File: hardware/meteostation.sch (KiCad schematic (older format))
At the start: 19 parts

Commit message: Annotation complete
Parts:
- gave numbers to parts that had none: 19
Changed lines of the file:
@@
 $EndDescr
 $Comp
-L Device:C C?
+L Device:C C7
 U 1 1 6032A8FA
 P 10250 3050
-F 0 "C?" H 10365 3096 50  0000 L CNN
+F 0 "C7" H 10365 3096 50  0000 L CNN
 F 1 "100nF" H 10365 3005 50  0000 L CNN
 F 2 "" H 10288 2900 50  0001 C CNN
@@
 $EndComp
 $Comp
-L power:GND #PWR0103
+L power:GND #PWR017
 U 1 1 6032C2F4
 P 10250 3300
-F 0 "#PWR0103" H 10250 3050 50  0001 C CNN
+F 0 "#PWR017" H 10250 3050 50  0001 C CNN
 F 1 "GND" H 10255 3127 50  0000 C CNN
 F 2 "" H 10250 3300 50  0001 C CNN
@@
 $EndComp
 $Comp
-L Device:C C?
+L Device:C C6
 U 1 1 60328012
 P 9750 3050
-F 0 "C?" H 9865 3096 50  0000 L CNN
+F 0 "C6" H 9865 3096 50  0000 L CNN
 F 1 "100nF" H 9865 3005 50  0000 L CNN
 F 2 "" H 9788 2900 50  0001 C CNN
@@
 $EndComp
 $Comp
-L Switch:SW_MEC_5G SW?
+L Switch:SW_MEC_5G SW1
 U 1 1 6035A760
 P 5750 2750
-F 0 "SW?" H 5750 3035 50  0000 C CNN
+F 0 "SW1" H 5750 3035 50  0000 C CNN
 F 1 "RESET_BTN" H 5800 2950 50  0000 C CNN
 F 2 "" H 5750 2950 50  0001 C CNN
@@
 $EndComp
 $Comp
-L Device:C C?
+L Device:C C5
 U 1 1 60360E03
 P 5750 3050
-F 0 "C?" V 5498 3050 50  0000 C CNN
+F 0 "C5" V 5498 3050 50  0000 C CNN
 F 1 "100nF" V 5589 3050 50  0000 C CNN
 F 2 "" H 5788 2900 50  0001 C CNN
@@
 	6050 2750 6050 2900
 $Comp
-L power:GND #PWR0107
+L power:GND #PWR016
 U 1 1 603644F2
 P 5450 3150
-F 0 "#PWR0107" H 5450 2900 50  0001 C CNN
+F 0 "#PWR016" H 5450 2900 50  0001 C CNN
 F 1 "GND" H 5455 2977 50  0000 C CNN
 F 2 "" H 5450 3150 50  0001 C CNN
@@
 $EndSheet
 $Comp
-L power:+3.3V #PWR0102
+L power:+3.3V #PWR015
 U 1 1 603A52DC
 P 10250 2800
-F 0 "#PWR0102" H 10250 2650 50  0001 C CNN
+F 0 "#PWR015" H 10250 2650 50  0001 C CNN
 F 1 "+3.3V" H 10265 2973 50  0000 C CNN
 F 2 "" H 10250 2800 50  0001 C CNN
@@
 $EndComp
 $Comp
-L MCU_ST_STM32L4:STM32L432KBUx U?
+L MCU_ST_STM32L4:STM32L432KBUx U1
 U 1 1 604F928D
 P 7750 3600
-F 0 "U?" H 7400 4500 50  0000 C CNN
+F 0 "U1" H 7400 4500 50  0000 C CNN
 F 1 "STM32L432KBUx" H 8250 2600 50  0000 C CNN
 F 2 "Package_DFN_QFN:QFN-32-1EP_5x5mm_P0.5mm_EP3.45x3.45mm" H 7350 2700 50  0001 R CNN
@@
 P 1550 3050
 AR Path="/60322A2E/6065CC0F" Ref="R?"  Part="1"
-AR Path="/6065CC0F" Ref="R?"  Part="1"
-F 0 "R?" V 1343 3050 50  0000 C CNN
+AR Path="/6065CC0F" Ref="R4"  Part="1"
+F 0 "R4" V 1343 3050 50  0000 C CNN
 F 1 "100R" V 1434 3050 50  0000 C CNN
 F 2 "" V 1480 3050 50  0001 C CNN
@@
 P 3550 6200
 AR Path="/60322A2E/60660547" Ref="R?"  Part="1"
-AR Path="/60660547" Ref="R?"  Part="1"
-F 0 "R?" V 3343 6200 50  0000 C CNN
+AR Path="/60660547" Ref="R6"  Part="1"
+F 0 "R6" V 3343 6200 50  0000 C CNN
 F 1 "100R" V 3434 6200 50  0000 C CNN
 F 2 "" V 3480 6200 50  0001 C CNN
@@
 	3000 6200 3400 6200
 $Comp
-L power:+3.3V #PWR0101
+L power:+3.3V #PWR014
 U 1 1 60665343
 P 7750 2550
-F 0 "#PWR0101" H 7750 2400 50  0001 C CNN
+F 0 "#PWR014" H 7750 2400 50  0001 C CNN
 F 1 "+3.3V" H 7765 2723 50  0000 C CNN
 F 2 "" H 7750 2550 50  0001 C CNN
@@
 	7750 4600 7850 4600
 $Comp
-L power:GND #PWR0108
+L power:GND #PWR020
 U 1 1 60667B8E
 P 7750 4600
-F 0 "#PWR0108" H 7750 4350 50  0001 C CNN
+F 0 "#PWR020" H 7750 4350 50  0001 C CNN
 F 1 "GND" H 7755 4427 50  0000 C CNN
 F 2 "" H 7750 4600 50  0001 C CNN
@@
 Connection ~ 5450 3050
 $Comp
-L Device:R R?
+L Device:R R3
 U 1 1 606B8930
 P 6950 2700
-F 0 "R?" H 7020 2746 50  0000 L CNN
+F 0 "R3" H 7020 2746 50  0000 L CNN
 F 1 "10K" H 7020 2655 50  0000 L CNN
 F 2 "" V 6880 2700 50  0001 C CNN
@@
 $EndComp
 $Comp
-L power:+3.3V #PWR0168
+L power:+3.3V #PWR013
 U 1 1 606B9473
 P 6950 2550
-F 0 "#PWR0168" H 6950 2400 50  0001 C CNN
+F 0 "#PWR013" H 6950 2400 50  0001 C CNN
 F 1 "+3.3V" H 6965 2723 50  0000 C CNN
 F 2 "" H 6950 2550 50  0001 C CNN
@@
 SWDIO
 $Comp
-L Connector:Conn_01x04_Male J?
+L Connector:Conn_01x04_Male J1
 U 1 1 606CCAFD
 P 9600 4150
-F 0 "J?" H 9550 4350 50  0000 C CNN
+F 0 "J1" H 9550 4350 50  0000 C CNN
 F 1 "PROG_Conn" H 9500 3900 50  0000 C CNN
 F 2 "" H 9600 4150 50  0001 C CNN
@@
 $EndComp
 $Comp
-L power:GND #PWR0169
+L power:GND #PWR019
 U 1 1 606CEFC8
 P 9800 4350
-F 0 "#PWR0169" H 9800 4100 50  0001 C CNN
+F 0 "#PWR019" H 9800 4100 50  0001 C CNN
 F 1 "GND" H 9805 4177 50  0000 C CNN
 F 2 "" H 9800 4350 50  0001 C CNN
@@
 SWCLK
 $Comp
-L power:GND #PWR0170
+L power:GND #PWR018
 U 1 1 606D3C7E
 P 6350 3350
-F 0 "#PWR0170" H 6350 3100 50  0001 C CNN
+F 0 "#PWR018" H 6350 3100 50  0001 C CNN
 F 1 "GND" H 6355 3177 50  0000 C CNN
 F 2 "" H 6350 3350 50  0001 C CNN
@@
 BQ25895_INT
 $Comp
-L Device:C C?
+L Device:C C8
 U 1 1 605E0A5B
 P 10750 3050
-F 0 "C?" H 10865 3096 50  0000 L CNN
+F 0 "C8" H 10865 3096 50  0000 L CNN
 F 1 "100nF" H 10865 3005 50  0000 L CNN
 F 2 "" H 10788 2900 50  0001 C CNN
@@
 STM_RX1-DIO1
 $Comp
-L Oscillator:SG-7050CAN X?
+L Oscillator:SG-7050CAN X1
 U 1 1 609D7D66
 P 6000 1300
-F 0 "X?" H 5800 1600 50  0000 L CNN
+F 0 "X1" H 5800 1600 50  0000 L CNN
 F 1 "YSO110TR_8MHz_10ppm" H 5350 1000 50  0000 L CNN
 F 2 "Oscillator:Oscillator_SMD_SeikoEpson_SG8002CA-4Pin_7.0x5.0mm" H 6700 950 50  0001 C CNN
@@
 $EndComp
 $Comp
-L power:+3.3V #PWR?
+L power:+3.3V #PWR03
 U 1 1 609DA287
 P 6000 1000
-F 0 "#PWR?" H 6000 850 50  0001 C CNN
+F 0 "#PWR03" H 6000 850 50  0001 C CNN
 F 1 "+3.3V" H 6015 1173 50  0000 C CNN
 F 2 "" H 6000 1000 50  0001 C CNN
@@
 $EndComp
 $Comp
-L power:GND #PWR?
+L power:GND #PWR09
 U 1 1 609DA80E
 P 6000 1600
-F 0 "#PWR?" H 6000 1350 50  0001 C CNN
+F 0 "#PWR09" H 6000 1350 50  0001 C CNN
 F 1 "GND" H 6005 1427 50  0000 C CNN
 F 2 "" H 6000 1600 50  0001 C CNN
@@
 $EndComp
 $Comp
-L Device:C C?
+L Device:C C2
 U 1 1 609DB544
 P 5050 1250
-F 0 "C?" H 5165 1296 50  0000 L CNN
+F 0 "C2" H 5165 1296 50  0000 L CNN
 F 1 "100nF" H 5165 1205 50  0000 L CNN
 F 2 "" H 5088 1100 50  0001 C CNN
@@
 $EndComp
 $Comp
-L power:+3.3V #PWR?
+L power:+3.3V #PWR06
 U 1 1 609DC7C1
 P 5050 1100
-F 0 "#PWR?" H 5050 950 50  0001 C CNN
+F 0 "#PWR06" H 5050 950 50  0001 C CNN
 F 1 "+3.3V" H 5065 1273 50  0000 C CNN
 F 2 "" H 5050 1100 50  0001 C CNN
@@
 $EndComp
 $Comp
-L power:GND #PWR?
+L power:GND #PWR08
 U 1 1 609DCF04
 P 5050 1400
-F 0 "#PWR?" H 5050 1150 50  0001 C CNN
+F 0 "#PWR08" H 5050 1150 50  0001 C CNN
 F 1 "GND" H 5055 1227 50  0000 C CNN
 F 2 "" H 5050 1400 50  0001 C CNN
@@
 $EndComp
 $Comp
-L Device:R R?
+L Device:R R1
 U 1 1 609DFF35
 P 5500 1100
-F 0 "R?" H 5570 1146 50  0000 L CNN
+F 0 "R1" H 5570 1146 50  0000 L CNN
 F 1 "10K" H 5570 1055 50  0000 L CNN
 F 2 "" V 5430 1100 50  0001 C CNN
@@
 	5500 1300 5500 1250
 $Comp
-L power:+3.3V #PWR?
+L power:+3.3V #PWR01
 U 1 1 609E1444
 P 5500 950
-F 0 "#PWR?" H 5500 800 50  0001 C CNN
+F 0 "#PWR01" H 5500 800 50  0001 C CNN
 F 1 "+3.3V" H 5515 1123 50  0000 C CNN
 F 2 "" H 5500 950 50  0001 C CNN
@@
 $EndComp
 $Comp
-L Device:C C?
+L Device:C C3
 U 1 1 609E3E78
 P 6450 1450
-F 0 "C?" H 6565 1496 50  0000 L CNN
+F 0 "C3" H 6565 1496 50  0000 L CNN
 F 1 "15pF" H 6565 1405 50  0000 L CNN
 F 2 "" H 6488 1300 50  0001 C CNN
@@
 $EndComp
 $Comp
-L power:GND #PWR?
+L power:GND #PWR010
 U 1 1 609E56B1
 P 6450 1600
-F 0 "#PWR?" H 6450 1350 50  0001 C CNN
+F 0 "#PWR010" H 6450 1350 50  0001 C CNN
 F 1 "GND" H 6455 1427 50  0000 C CNN
 F 2 "" H 6450 1600 50  0001 C CNN
@@
 $EndComp
 $Comp
-L Oscillator:ECS-2520MV-xxx-xx X?
+L Oscillator:ECS-2520MV-xxx-xx X2
 U 1 1 609E74E4
 P 8750 1300
-F 0 "X?" H 8450 1600 50  0000 L CNN
+F 0 "X2" H 8450 1600 50  0000 L CNN
 F 1 "YSO120TK_32.768KHz_10ppm" H 7900 1000 50  0000 L CNN
 F 2 "Oscillator:Oscillator_SMD_ECS_2520MV-xxx-xx-4Pin_2.5x2.0mm" H 9200 950 50  0001 C CNN
@@
 $EndComp
 $Comp
-L Device:C C?
+L Device:C C1
 U 1 1 609EB7F3
 P 7700 1150
-F 0 "C?" H 7815 1196 50  0000 L CNN
+F 0 "C1" H 7815 1196 50  0000 L CNN
 F 1 "100nF" H 7815 1105 50  0000 L CNN
 F 2 "" H 7738 1000 50  0001 C CNN
@@
 $EndComp
 $Comp
-L power:+3.3V #PWR?
+L power:+3.3V #PWR04
 U 1 1 609EB7F9
 P 7700 1000
-F 0 "#PWR?" H 7700 850 50  0001 C CNN
+F 0 "#PWR04" H 7700 850 50  0001 C CNN
 F 1 "+3.3V" H 7715 1173 50  0000 C CNN
 F 2 "" H 7700 1000 50  0001 C CNN
@@
 $EndComp
 $Comp
-L power:GND #PWR?
+L power:GND #PWR07
 U 1 1 609EB7FF
 P 7700 1300
-F 0 "#PWR?" H 7700 1050 50  0001 C CNN
+F 0 "#PWR07" H 7700 1050 50  0001 C CNN
 F 1 "GND" H 7705 1127 50  0000 C CNN
 F 2 "" H 7700 1300 50  0001 C CNN
@@
 $EndComp
 $Comp
-L Device:R R?
+L Device:R R2
 U 1 1 609ED2E4
 P 8200 1100
-F 0 "R?" H 8270 1146 50  0000 L CNN
+F 0 "R2" H 8270 1146 50  0000 L CNN
 F 1 "10K" H 8270 1055 50  0000 L CNN
 F 2 "" V 8130 1100 50  0001 C CNN
@@
 $EndComp
 $Comp
-L power:+3.3V #PWR?
+L power:+3.3V #PWR02
 U 1 1 609ED2EA
 P 8200 950
-F 0 "#PWR?" H 8200 800 50  0001 C CNN
+F 0 "#PWR02" H 8200 800 50  0001 C CNN
 F 1 "+3.3V" H 8215 1123 50  0000 C CNN
 F 2 "" H 8200 950 50  0001 C CNN
@@
 HSE
 $Comp
-L power:GND #PWR?
+L power:GND #PWR011
 U 1 1 60A1176F
 P 8750 1600
-F 0 "#PWR?" H 8750 1350 50  0001 C CNN
+F 0 "#PWR011" H 8750 1350 50  0001 C CNN
 F 1 "GND" H 8755 1427 50  0000 C CNN
 F 2 "" H 8750 1600 50  0001 C CNN
@@
 $EndComp
 $Comp
-L Device:C C?
+L Device:C C4
 U 1 1 60A13465
 P 9300 1450
-F 0 "C?" H 9415 1496 50  0000 L CNN
+F 0 "C4" H 9415 1496 50  0000 L CNN
 F 1 "15pF" H 9415 1405 50  0000 L CNN
 F 2 "" H 9338 1300 50  0001 C CNN
@@
 $EndComp
 $Comp
-L power:GND #PWR?
+L power:GND #PWR012
 U 1 1 60A1346B
 P 9300 1600
-F 0 "#PWR?" H 9300 1350 50  0001 C CNN
+F 0 "#PWR012" H 9300 1350 50  0001 C CNN
 F 1 "GND" H 9305 1427 50  0000 C CNN
 F 2 "" H 9300 1600 50  0001 C CNN
@@
 LSE
 $Comp
-L power:+3.3V #PWR?
+L power:+3.3V #PWR05
 U 1 1 60A13B82
 P 8750 1000
-F 0 "#PWR?" H 8750 850 50  0001 C CNN
+F 0 "#PWR05" H 8750 850 50  0001 C CNN
 F 1 "+3.3V" H 8765 1173 50  0000 C CNN
 F 2 "" H 8750 1000 50  0001 C CNN
@@
 	6950 2900 7250 2900
 $Comp
-L Device:R R?
+L Device:R R5
 U 1 1 60A1EB5C
 P 6800 3300
-F 0 "R?" V 6593 3300 50  0000 C CNN
+F 0 "R5" V 6593 3300 50  0000 C CNN
 F 1 "10K" V 6684 3300 50  0000 C CNN
 F 2 "" V 6730 3300 50  0001 C CNN

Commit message: Finish adding footprints
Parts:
- C1, C2, C3, C4, C5, C6, C7, C8: footprint (none) -> Capacitor_SMD:C_0805_2012Metric
- J1: footprint (none) -> Connector_PinHeader_2.54mm:PinHeader_1x04_P2.54mm_Vertical
- R1, R2, R3, R4, R5, R6: footprint (none) -> Resistor_SMD:R_0805_2012Metric
- SW1: footprint (none) -> libs:SW_TS-1187A-B-A-B
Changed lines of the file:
@@
 F 0 "C7" H 10365 3096 50  0000 L CNN
 F 1 "100nF" H 10365 3005 50  0000 L CNN
-F 2 "" H 10288 2900 50  0001 C CNN
+F 2 "Capacitor_SMD:C_0805_2012Metric" H 10288 2900 50  0001 C CNN
 F 3 "~" H 10250 3050 50  0001 C CNN
 	1    10250 3050
@@
 F 0 "C6" H 9865 3096 50  0000 L CNN
 F 1 "100nF" H 9865 3005 50  0000 L CNN
-F 2 "" H 9788 2900 50  0001 C CNN
+F 2 "Capacitor_SMD:C_0805_2012Metric" H 9788 2900 50  0001 C CNN
 F 3 "~" H 9750 3050 50  0001 C CNN
 	1    9750 3050
@@
 F 0 "SW1" H 5750 3035 50  0000 C CNN
 F 1 "RESET_BTN" H 5800 2950 50  0000 C CNN
-F 2 "" H 5750 2950 50  0001 C CNN
+F 2 "libs:SW_TS-1187A-B-A-B" H 5750 2950 50  0001 C CNN
 F 3 "http://www.apem.com/int/index.php?controller=attachment&id_attachment=488" H 5750 2950 50  0001 C CNN
 	1    5750 2750
@@
 F 0 "C5" V 5498 3050 50  0000 C CNN
 F 1 "100nF" V 5589 3050 50  0000 C CNN
-F 2 "" H 5788 2900 50  0001 C CNN
+F 2 "Capacitor_SMD:C_0805_2012Metric" H 5788 2900 50  0001 C CNN
 F 3 "~" H 5750 3050 50  0001 C CNN
 	1    5750 3050
@@
 F 0 "R4" V 1343 3050 50  0000 C CNN
 F 1 "100R" V 1434 3050 50  0000 C CNN
-F 2 "" V 1480 3050 50  0001 C CNN
+F 2 "Resistor_SMD:R_0805_2012Metric" V 1480 3050 50  0001 C CNN
 F 3 "~" H 1550 3050 50  0001 C CNN
 	1    1550 3050
@@
 F 0 "R6" V 3343 6200 50  0000 C CNN
 F 1 "100R" V 3434 6200 50  0000 C CNN
-F 2 "" V 3480 6200 50  0001 C CNN
+F 2 "Resistor_SMD:R_0805_2012Metric" V 3480 6200 50  0001 C CNN
 F 3 "~" H 3550 6200 50  0001 C CNN
 	1    3550 6200
@@
 F 0 "R3" H 7020 2746 50  0000 L CNN
 F 1 "10K" H 7020 2655 50  0000 L CNN
-F 2 "" V 6880 2700 50  0001 C CNN
+F 2 "Resistor_SMD:R_0805_2012Metric" V 6880 2700 50  0001 C CNN
 F 3 "~" H 6950 2700 50  0001 C CNN
 	1    6950 2700
@@
 F 0 "J1" H 9550 4350 50  0000 C CNN
 F 1 "PROG_Conn" H 9500 3900 50  0000 C CNN
-F 2 "" H 9600 4150 50  0001 C CNN
+F 2 "Connector_PinHeader_2.54mm:PinHeader_1x04_P2.54mm_Vertical" H 9600 4150 50  0001 C CNN
 F 3 "~" H 9600 4150 50  0001 C CNN
 	1    9600 4150
@@
 F 0 "C8" H 10865 3096 50  0000 L CNN
 F 1 "100nF" H 10865 3005 50  0000 L CNN
-F 2 "" H 10788 2900 50  0001 C CNN
+F 2 "Capacitor_SMD:C_0805_2012Metric" H 10788 2900 50  0001 C CNN
 F 3 "~" H 10750 3050 50  0001 C CNN
 	1    10750 3050
@@
 F 0 "C2" H 5165 1296 50  0000 L CNN
 F 1 "100nF" H 5165 1205 50  0000 L CNN
-F 2 "" H 5088 1100 50  0001 C CNN
+F 2 "Capacitor_SMD:C_0805_2012Metric" H 5088 1100 50  0001 C CNN
 F 3 "~" H 5050 1250 50  0001 C CNN
 	1    5050 1250
@@
 F 0 "R1" H 5570 1146 50  0000 L CNN
 F 1 "10K" H 5570 1055 50  0000 L CNN
-F 2 "" V 5430 1100 50  0001 C CNN
+F 2 "Resistor_SMD:R_0805_2012Metric" V 5430 1100 50  0001 C CNN
 F 3 "~" H 5500 1100 50  0001 C CNN
 	1    5500 1100
@@
 F 0 "C3" H 6565 1496 50  0000 L CNN
 F 1 "15pF" H 6565 1405 50  0000 L CNN
-F 2 "" H 6488 1300 50  0001 C CNN
+F 2 "Capacitor_SMD:C_0805_2012Metric" H 6488 1300 50  0001 C CNN
 F 3 "~" H 6450 1450 50  0001 C CNN
 	1    6450 1450
@@
 F 0 "C1" H 7815 1196 50  0000 L CNN
 F 1 "100nF" H 7815 1105 50  0000 L CNN
-F 2 "" H 7738 1000 50  0001 C CNN
+F 2 "Capacitor_SMD:C_0805_2012Metric" H 7738 1000 50  0001 C CNN
 F 3 "~" H 7700 1150 50  0001 C CNN
 	1    7700 1150
@@
 F 0 "R2" H 8270 1146 50  0000 L CNN
 F 1 "10K" H 8270 1055 50  0000 L CNN
-F 2 "" V 8130 1100 50  0001 C CNN
+F 2 "Resistor_SMD:R_0805_2012Metric" V 8130 1100 50  0001 C CNN
 F 3 "~" H 8200 1100 50  0001 C CNN
 	1    8200 1100
@@
 F 0 "C4" H 9415 1496 50  0000 L CNN
 F 1 "15pF" H 9415 1405 50  0000 L CNN
-F 2 "" H 9338 1300 50  0001 C CNN
+F 2 "Capacitor_SMD:C_0805_2012Metric" H 9338 1300 50  0001 C CNN
 F 3 "~" H 9300 1450 50  0001 C CNN
 	1    9300 1450
@@
 F 0 "R5" V 6593 3300 50  0000 C CNN
 F 1 "10K" V 6684 3300 50  0000 C CNN
-F 2 "" V 6730 3300 50  0001 C CNN
+F 2 "Resistor_SMD:R_0805_2012Metric" V 6730 3300 50  0001 C CNN
 F 3 "~" H 6800 3300 50  0001 C CNN
 	1    6800 3300

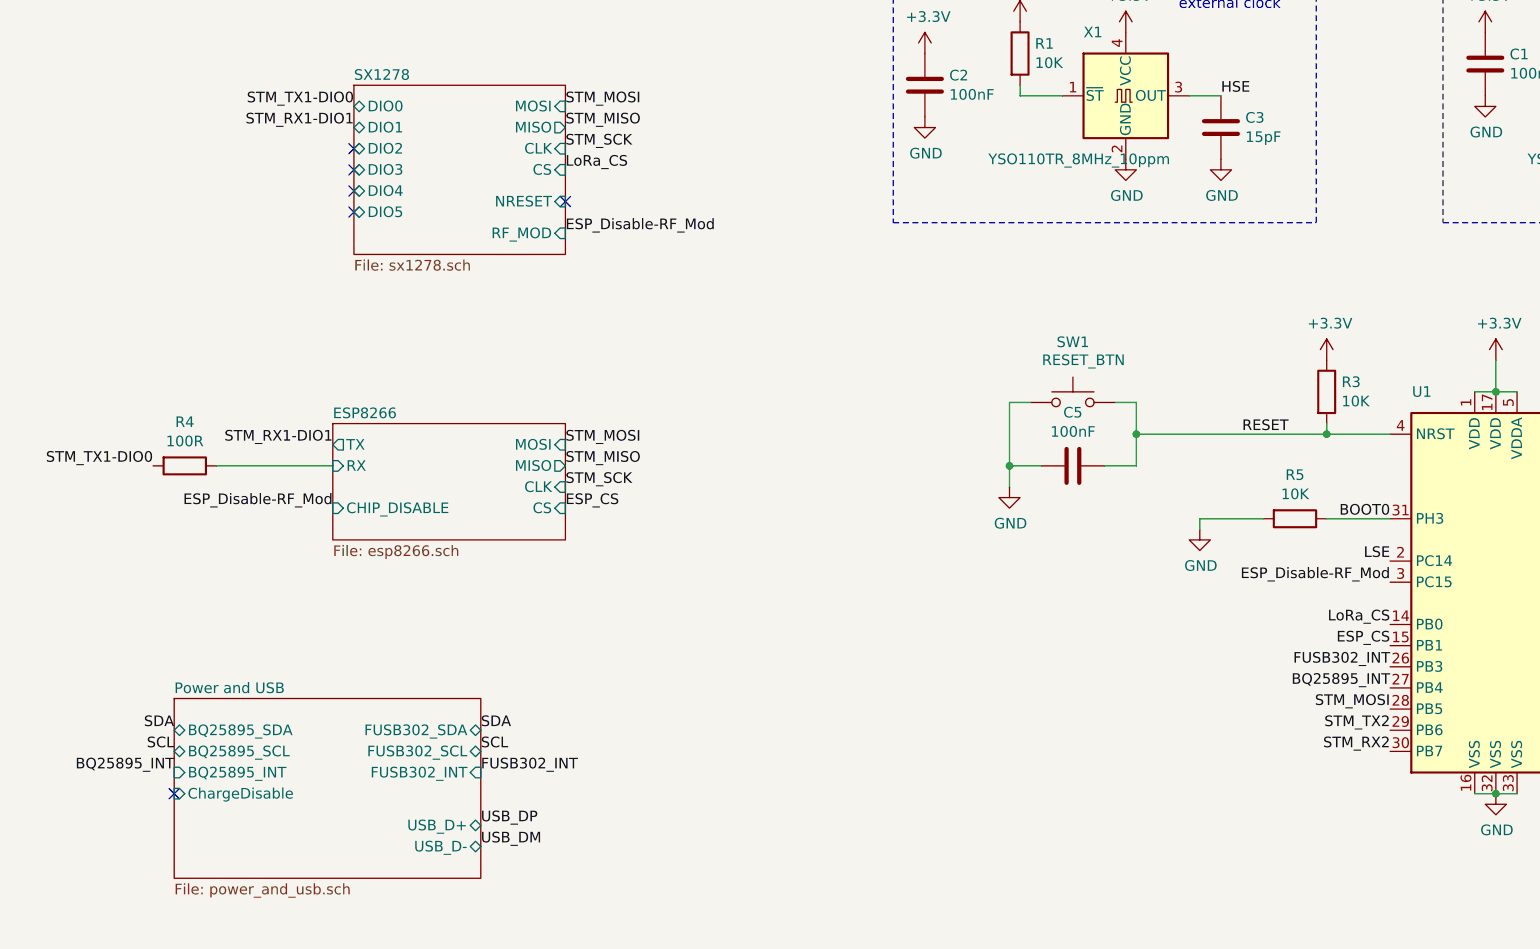
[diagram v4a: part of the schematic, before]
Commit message: Optimazed labels
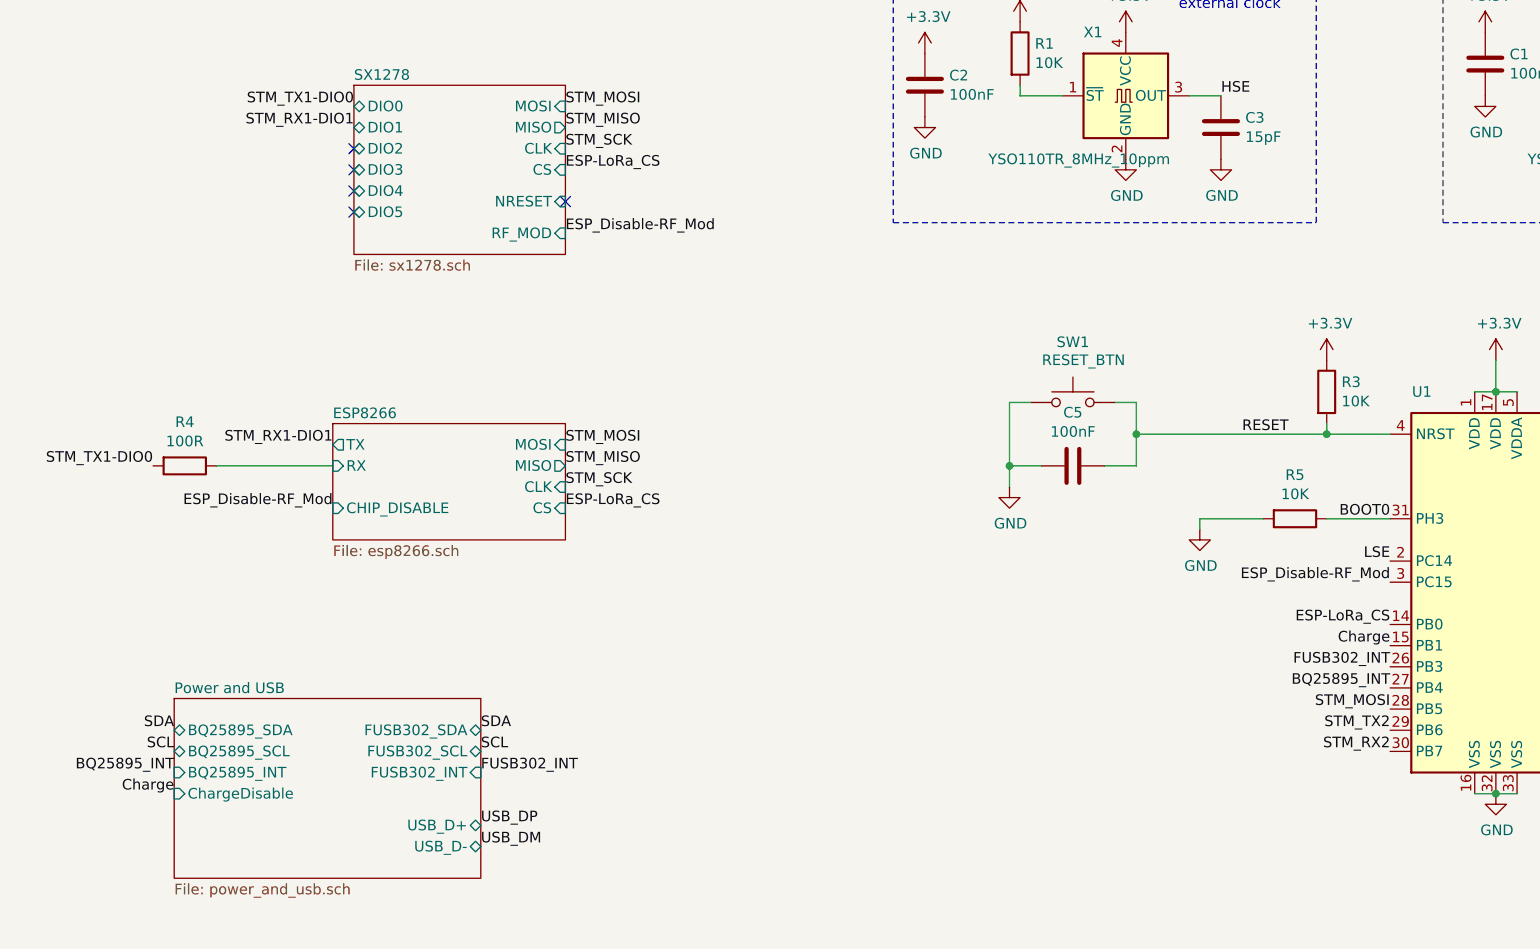
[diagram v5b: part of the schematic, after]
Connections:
- net ESP_CS renamed Charge
- net LoRa_CS renamed ESP-LoRa_CS
- no-connect marks 8 -> 7
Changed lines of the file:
@@
 MQ2
 Text Label 3350 3250 0    50   ~ 0
-ESP_CS
+ESP-LoRa_CS
 Text Label 3350 1650 0    50   ~ 0
-LoRa_CS
+ESP-LoRa_CS
 Text Label 7250 3800 2    50   ~ 0
-LoRa_CS
-Text Label 7250 3900 2    50   ~ 0
-ESP_CS
+ESP-LoRa_CS
 Text Label 7250 3600 2    50   ~ 0
 ESP_Disable-RF_Mod
@@
 Text Label 8250 4400 0    50   ~ 0
 Enable_MQ2
-NoConn ~ 1500 4600
 Text Label 2250 3250 2    50   ~ 0
 ESP_Disable-RF_Mod
@@
 Wire Wire Line
 	6350 3300 6650 3300
+Text Label 1500 4600 2    50   ~ 0
+Charge
+Text Label 7250 3900 2    50   ~ 0
+Charge
 $EndSCHEMATC

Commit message: Finished power PCB part
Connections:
- net USB_DM renamed USB_D-
- net USB_DP renamed USB_D+
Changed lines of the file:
@@
 Text Label 1500 4300 2    50   ~ 0
 SDA
-Text Label 8250 4100 0    50   ~ 0
-USB_DP
-Text Label 8250 4000 0    50   ~ 0
-USB_DM
 Text Label 2950 4750 0    50   ~ 0
-USB_DP
+USB_D+
 Text Label 2950 4850 0    50   ~ 0
-USB_DM
+USB_D-
 Text Label 8250 3100 0    50   ~ 0
 STM_TX1-DIO0
@@
 Text Label 7250 3900 2    50   ~ 0
 Charge
+Text Label 8250 4100 0    50   ~ 0
+USB_D+
+Text Label 8250 4000 0    50   ~ 0
+USB_D-
 $EndSCHEMATC
